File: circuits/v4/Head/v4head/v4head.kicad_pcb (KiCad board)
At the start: 4 copper layers, 82.5 x 39.4 mm, 21 parts

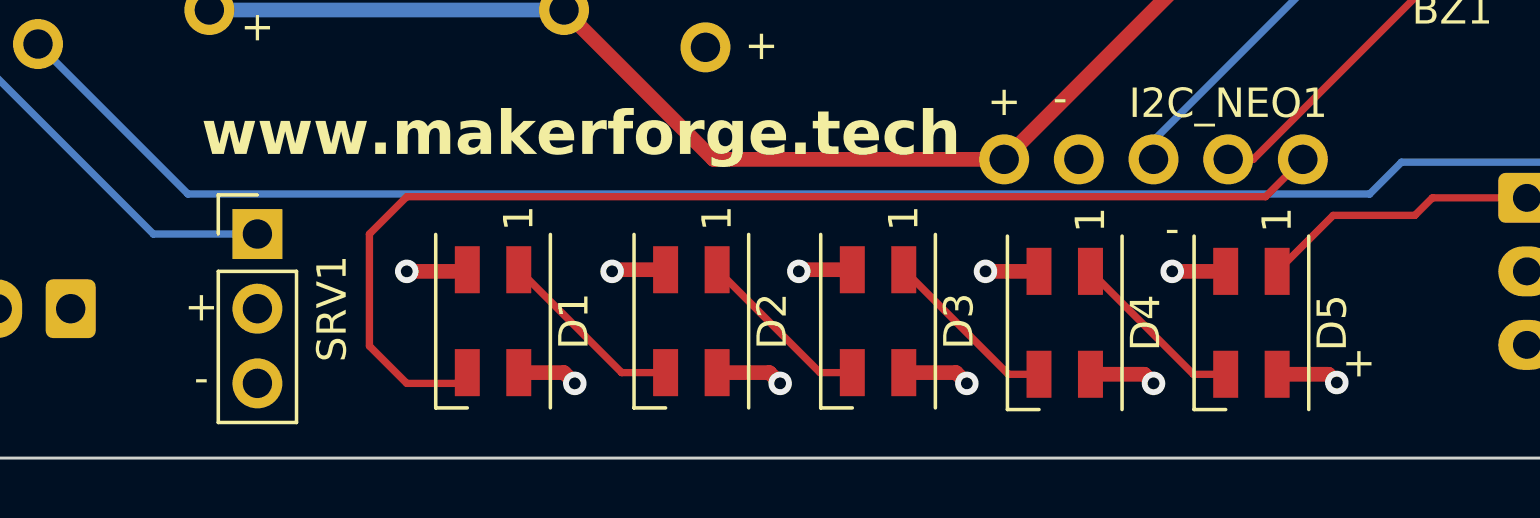
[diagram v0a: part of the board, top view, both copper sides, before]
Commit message: Final version 1.0. Added decoupling caps to neopixels.
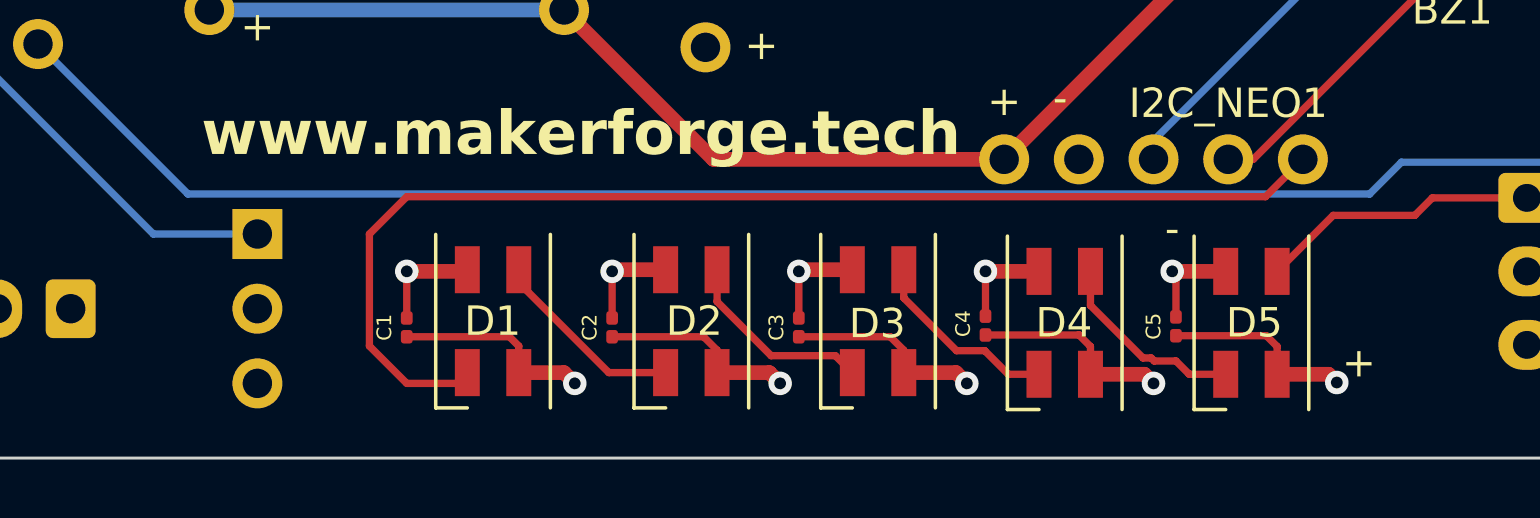
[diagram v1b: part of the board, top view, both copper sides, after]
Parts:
- added C1: C_Small, Capacitor_SMD:C_0201_0603Metric, F.Cu at (146.1, 83.2)
- added C2: C_Small, Capacitor_SMD:C_0201_0603Metric, F.Cu at (153.0, 83.2)
- added C3: C_Small, Capacitor_SMD:C_0201_0603Metric, F.Cu at (159.4, 83.2)
- added C4: C_Small, Capacitor_SMD:C_0201_0603Metric, F.Cu at (165.7, 83.1)
- added C5: C_Small, Capacitor_SMD:C_0201_0603Metric, F.Cu at (172.2, 83.1)
- SRV1: moved to B.Cu
- turned SRV1 to 180 degrees
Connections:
- D2 pad 1: Net-(D2-DOUT) -> GND
- D3 pad 1: Net-(D3-DOUT) -> GND
- D3 pad 3: Net-(D2-DOUT) -> GND
- D4 pad 1: Net-(D4-DOUT) -> GND
- D4 pad 3: Net-(D3-DOUT) -> GND
- D5 pad 3: Net-(D4-DOUT) -> GND
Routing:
- net GND: track 9.41 -> 37.3 mm
- net +5V: track 11.1 -> 34.2 mm
- net Net-(D3-DOUT): track 6.07 -> 0.00 mm
- net Net-(D2-DOUT): track 6.05 -> 0.00 mm
- net Net-(D4-DOUT): track 6.05 -> 0.00 mm

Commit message: Added version number
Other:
- board text added: "Pi Module Connector v1.0"
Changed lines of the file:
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@@
     (effects (font (size 1 1) (thickness 0.15)))
+  )
+  (gr_text "Pi Module Connector v1.0" (at 143.891 79.248) (layer "F.SilkS")
+    (effects (font (size 1 1) (thickness 0.15)) (justify left bottom))
   )
   (gr_text "+" (at 128.905 54.61 180) (layer "F.SilkS")
